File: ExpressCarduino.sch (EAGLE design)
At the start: 14 parts, among them IC1 MCP23017ML, U1 AP3012

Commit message: I keep tweaking the board...
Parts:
- renumbered U$2 to IC2
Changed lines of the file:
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@@
 <part name="GND5" library="supply1" deviceset="GND" device=""/>
 <part name="GPIO" library="SparkFun-Connectors" deviceset="M08" device=""/>
-<part name="U$2" library="HokieGeek" deviceset="SN74LV4051A" device=""/>
+<part name="IC2" library="HokieGeek" deviceset="SN74LV4051A" device=""/>
 <part name="ADC" library="SparkFun-Connectors" deviceset="M08" device=""/>
 <part name="IC1" library="adafruit" deviceset="MCP23017" device="ML"/>
@@
 <instance part="GND5" gate="1" x="127" y="76.2"/>
 <instance part="GPIO" gate="G$1" x="88.9" y="104.14" rot="R180"/>
-<instance part="U$2" gate="G$1" x="127" y="99.06"/>
+<instance part="IC2" gate="G$1" x="127" y="99.06"/>
 <instance part="ADC" gate="G$1" x="147.32" y="101.6" rot="R180"/>
 <instance part="IC1" gate="G$1" x="68.58" y="88.9"/>
@@
 </segment>
 <segment>
-<pinref part="U$2" gate="G$1" pin="VCC"/>
+<pinref part="IC2" gate="G$1" pin="VCC"/>
 <wire x1="127" y1="116.84" x2="127" y2="119.38" width="0.1524" layer="91"/>
 <label x="127" y="119.38" size="1.778" layer="95"/>
@@
 </segment>
 <segment>
-<pinref part="U$2" gate="G$1" pin="GND"/>
+<pinref part="IC2" gate="G$1" pin="GND"/>
 <pinref part="GND5" gate="1" pin="GND"/>
 <wire x1="127" y1="78.74" x2="127" y2="81.28" width="0.1524" layer="91"/>
@@
 </segment>
 <segment>
-<pinref part="U$2" gate="G$1" pin="!EN"/>
+<pinref part="IC2" gate="G$1" pin="!EN"/>
 <wire x1="111.76" y1="88.9" x2="106.68" y2="88.9" width="0.1524" layer="91"/>
 <label x="104.14" y="88.9" size="1.778" layer="95"/>
@@
 <net name="N$19" class="0">
 <segment>
-<pinref part="U$2" gate="G$1" pin="Y0"/>
+<pinref part="IC2" gate="G$1" pin="Y0"/>
 <pinref part="ADC" gate="G$1" pin="1"/>
 </segment>
@@
 <net name="N$20" class="0">
 <segment>
-<pinref part="U$2" gate="G$1" pin="Y1"/>
+<pinref part="IC2" gate="G$1" pin="Y1"/>
 <pinref part="ADC" gate="G$1" pin="2"/>
 </segment>
@@
 <net name="N$21" class="0">
 <segment>
-<pinref part="U$2" gate="G$1" pin="Y2"/>
+<pinref part="IC2" gate="G$1" pin="Y2"/>
 <pinref part="ADC" gate="G$1" pin="3"/>
 </segment>
@@
 <net name="N$22" class="0">
 <segment>
-<pinref part="U$2" gate="G$1" pin="Y3"/>
+<pinref part="IC2" gate="G$1" pin="Y3"/>
 <pinref part="ADC" gate="G$1" pin="4"/>
 </segment>
@@
 <net name="N$23" class="0">
 <segment>
-<pinref part="U$2" gate="G$1" pin="Y4"/>
+<pinref part="IC2" gate="G$1" pin="Y4"/>
 <pinref part="ADC" gate="G$1" pin="5"/>
 </segment>
@@
 <net name="N$24" class="0">
 <segment>
-<pinref part="U$2" gate="G$1" pin="Y5"/>
+<pinref part="IC2" gate="G$1" pin="Y5"/>
 <pinref part="ADC" gate="G$1" pin="6"/>
 </segment>
@@
 <net name="N$25" class="0">
 <segment>
-<pinref part="U$2" gate="G$1" pin="Y6"/>
+<pinref part="IC2" gate="G$1" pin="Y6"/>
 <pinref part="ADC" gate="G$1" pin="7"/>
 </segment>
@@
 <net name="N$26" class="0">
 <segment>
-<pinref part="U$2" gate="G$1" pin="Y7"/>
+<pinref part="IC2" gate="G$1" pin="Y7"/>
 <pinref part="ADC" gate="G$1" pin="8"/>
 </segment>
@@
 </segment>
 <segment>
-<pinref part="U$2" gate="G$1" pin="COM"/>
+<pinref part="IC2" gate="G$1" pin="COM"/>
 <wire x1="109.22" y1="96.52" x2="111.76" y2="96.52" width="0.1524" layer="91"/>
 <label x="99.06" y="96.52" size="1.778" layer="95"/>
@@
 <net name="MUX_A" class="0">
 <segment>
-<pinref part="U$2" gate="G$1" pin="A"/>
+<pinref part="IC2" gate="G$1" pin="A"/>
 <wire x1="111.76" y1="109.22" x2="109.22" y2="109.22" width="0.1524" layer="91"/>
 <label x="104.14" y="109.22" size="1.778" layer="95"/>
@@
 <net name="MUX_B" class="0">
 <segment>
-<pinref part="U$2" gate="G$1" pin="B"/>
+<pinref part="IC2" gate="G$1" pin="B"/>
 <wire x1="111.76" y1="106.68" x2="109.22" y2="106.68" width="0.1524" layer="91"/>
 <label x="104.14" y="106.68" size="1.778" layer="95"/>
@@
 <net name="MUX_C" class="0">
 <segment>
-<pinref part="U$2" gate="G$1" pin="C"/>
+<pinref part="IC2" gate="G$1" pin="C"/>
 <wire x1="111.76" y1="104.14" x2="109.22" y2="104.14" width="0.1524" layer="91"/>
 <label x="104.14" y="104.14" size="1.778" layer="95"/>

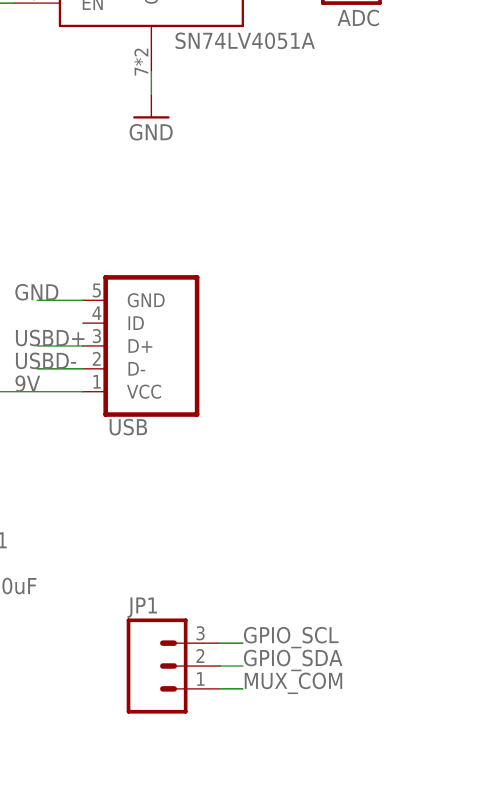
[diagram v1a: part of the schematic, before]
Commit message: Added power supply pins based on #10
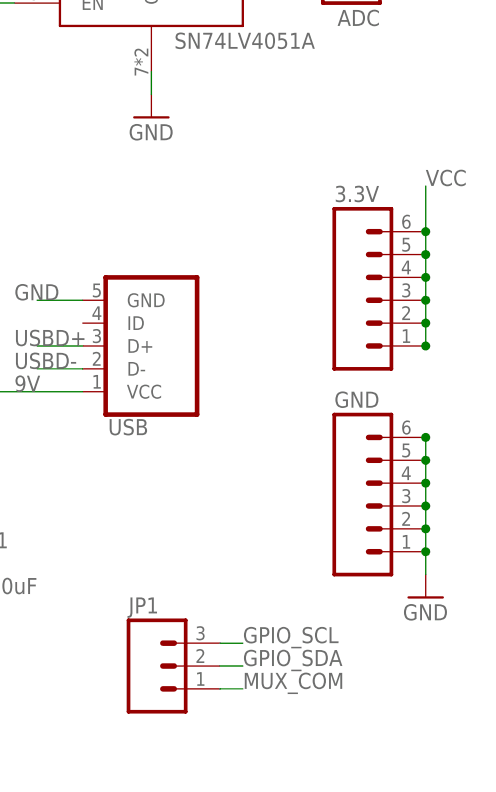
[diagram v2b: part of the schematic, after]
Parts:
- added 3.3V, GND: (no value), SparkFun-Connectors:M06SILK_FEMALE_PTH
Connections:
- net GND: now also GND.1, GND.2, GND.3, GND.4, GND.5, GND.6
- net VCC: now also 3.3V.1, 3.3V.2, 3.3V.3, 3.3V.4, 3.3V.5, 3.3V.6
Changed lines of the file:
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@@
 <part name="IC1" library="adafruit" deviceset="MCP23017" device="ML"/>
 <part name="JP1" library="SparkFun-Connectors" deviceset="M03" device="PTH"/>
+<part name="3.3V" library="SparkFun-Connectors" deviceset="M06" device="SILK_FEMALE_PTH"/>
+<part name="GND" library="SparkFun-Connectors" deviceset="M06" device="SILK_FEMALE_PTH"/>
+<part name="GND2" library="supply1" deviceset="GND" device=""/>
 </parts>
 <sheets>
@@
 <instance part="IC1" gate="G$1" x="68.58" y="88.9"/>
 <instance part="JP1" gate="G$1" x="127" y="15.24"/>
+<instance part="3.3V" gate="G$1" x="152.4" y="55.88"/>
+<instance part="GND" gate="G$1" x="152.4" y="33.02"/>
+<instance part="GND2" gate="1" x="157.48" y="22.86"/>
 </instances>
 <busses>
@@
 <wire x1="53.34" y1="104.14" x2="53.34" y2="109.22" width="0.1524" layer="91"/>
 <junction x="53.34" y="109.22"/>
+</segment>
+<segment>
+<pinref part="3.3V" gate="G$1" pin="1"/>
+<pinref part="3.3V" gate="G$1" pin="2"/>
+<wire x1="157.48" y1="50.8" x2="157.48" y2="53.34" width="0.1524" layer="91"/>
+<pinref part="3.3V" gate="G$1" pin="3"/>
+<wire x1="157.48" y1="53.34" x2="157.48" y2="55.88" width="0.1524" layer="91"/>
+<pinref part="3.3V" gate="G$1" pin="4"/>
+<wire x1="157.48" y1="55.88" x2="157.48" y2="58.42" width="0.1524" layer="91"/>
+<pinref part="3.3V" gate="G$1" pin="5"/>
+<wire x1="157.48" y1="58.42" x2="157.48" y2="60.96" width="0.1524" layer="91"/>
+<pinref part="3.3V" gate="G$1" pin="6"/>
+<wire x1="157.48" y1="60.96" x2="157.48" y2="63.5" width="0.1524" layer="91"/>
+<wire x1="157.48" y1="63.5" x2="157.48" y2="68.58" width="0.1524" layer="91"/>
+<label x="157.48" y="68.58" size="1.778" layer="95"/>
+<junction x="157.48" y="50.8"/>
+<junction x="157.48" y="53.34"/>
+<junction x="157.48" y="55.88"/>
+<junction x="157.48" y="58.42"/>
+<junction x="157.48" y="60.96"/>
+<junction x="157.48" y="63.5"/>
 </segment>
 </net>
@@
 <junction x="53.34" y="76.2"/>
 </segment>
+<segment>
+<pinref part="GND2" gate="1" pin="GND"/>
+<pinref part="GND" gate="G$1" pin="1"/>
+<wire x1="157.48" y1="25.4" x2="157.48" y2="27.94" width="0.1524" layer="91"/>
+<pinref part="GND" gate="G$1" pin="2"/>
+<wire x1="157.48" y1="27.94" x2="157.48" y2="30.48" width="0.1524" layer="91"/>
+<pinref part="GND" gate="G$1" pin="3"/>
+<wire x1="157.48" y1="30.48" x2="157.48" y2="33.02" width="0.1524" layer="91"/>
+<pinref part="GND" gate="G$1" pin="4"/>
+<wire x1="157.48" y1="33.02" x2="157.48" y2="35.56" width="0.1524" layer="91"/>
+<pinref part="GND" gate="G$1" pin="5"/>
+<wire x1="157.48" y1="35.56" x2="157.48" y2="38.1" width="0.1524" layer="91"/>
+<pinref part="GND" gate="G$1" pin="6"/>
+<wire x1="157.48" y1="38.1" x2="157.48" y2="40.64" width="0.1524" layer="91"/>
+<junction x="157.48" y="27.94"/>
+<junction x="157.48" y="30.48"/>
+<junction x="157.48" y="33.02"/>
+<junction x="157.48" y="35.56"/>
+<junction x="157.48" y="38.1"/>
+<junction x="157.48" y="40.64"/>
+</segment>
 </net>

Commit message: Trying things out
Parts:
- added IC3: MCP23008, HokieGeek:MCP23008
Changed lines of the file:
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@@
 <layer number="255" name="routoute" color="7" fill="1" visible="yes" active="yes"/>
 </layers>
-<schematic xreflabel="%F%N/%S.%C%R" xrefpart="/%S.%C%R">
+<schematic xreflabel="%F%N/%S" xrefpart="/%S">
 <attributes>
 </attributes>
@@
 <part name="GND" library="SparkFun-Connectors" deviceset="M06" device="SILK_FEMALE_PTH"/>
 <part name="GND2" library="supply1" deviceset="GND" device=""/>
+<part name="IC3" library="HokieGeek" deviceset="MCP23008" device=""/>
 </parts>
 <sheets>
@@
 <instance part="GND" gate="G$1" x="152.4" y="33.02"/>
 <instance part="GND2" gate="1" x="157.48" y="22.86"/>
+<instance part="IC3" gate="G$1" x="68.58" y="139.7"/>
 </instances>
 <busses>

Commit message: Modified current schematic to remove potential nogo and added "basic" board
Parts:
- removed IC3: MCP23008, HokieGeek:MCP23008
- IC2: value SN74LV4051A -> SN74LV4051APWR; device HokieGeek:SN74LV4051A -> HokieGeek:SN74LV4051APWR
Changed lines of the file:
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@@
 <?xml version="1.0" encoding="utf-8"?>
 <!DOCTYPE eagle SYSTEM "eagle.dtd">
-<eagle version="7.4.0">
+<eagle version="9.1.2">
 <drawing>
 <settings>
 <setting alwaysvectorfont="no"/>
+<setting keepoldvectorfont="yes"/>
 <setting verticaltext="up"/>
 </settings>
@@
 <part name="R1" library="SparkFun-Resistors" deviceset="0.22OHM-1/4W-1%(0805)" device="" value="41.2K"/>
 <part name="R2" library="SparkFun-Resistors" deviceset="0.22OHM-1/4W-1%(0805)" device="" value="6.5K"/>
-<part name="GND1" library="supply1" deviceset="GND" device=""/>
+<part name="GND1" library="supply1" library_urn="urn:adsk.eagle:library:371" deviceset="GND" device=""/>
 <part name="U1" library="HokieGeek" deviceset="AP3012" device="" value="AP3012"/>
-<part name="C1" library="SparkFun-Capacitors" deviceset="1.0UF-16V-10%(0603)" device="" value="1.0uF"/>
-<part name="C2" library="SparkFun-Capacitors" deviceset="1.0UF-16V-10%(0603)" device="" value="1.0uF"/>
+<part name="C1" library="SparkFun-Capacitors" library_urn="urn:adsk.eagle:library:510" deviceset="1.0UF-16V-10%(0603)" device="" value="1.0uF"/>
+<part name="C2" library="SparkFun-Capacitors" library_urn="urn:adsk.eagle:library:510" deviceset="1.0UF-16V-10%(0603)" device="" value="1.0uF"/>
 <part name="L1" library="SparkFun-Passives" deviceset="INDUCTOR" device="SDR0403-560KL" value="56uH"/>
 <part name="D1" library="HokieGeek" deviceset="DIODE-SCHOTTKY" device="" value="1N5819"/>
 <part name="USB" library="HokieGeek" deviceset="USB_MICROB_PLUG" device="&quot;"/>
-<part name="GND4" library="supply1" deviceset="GND" device=""/>
-<part name="GND5" library="supply1" deviceset="GND" device=""/>
+<part name="GND4" library="supply1" library_urn="urn:adsk.eagle:library:371" deviceset="GND" device=""/>
+<part name="GND5" library="supply1" library_urn="urn:adsk.eagle:library:371" deviceset="GND" device=""/>
 <part name="GPIO" library="SparkFun-Connectors" deviceset="M08" device=""/>
-<part name="IC2" library="HokieGeek" deviceset="SN74LV4051A" device=""/>
+<part name="IC2" library="HokieGeek" deviceset="SN74LV4051A" device="PWR"/>
 <part name="ADC" library="SparkFun-Connectors" deviceset="M08" device=""/>
-<part name="IC1" library="adafruit" deviceset="MCP23017" device="ML"/>
+<part name="IC1" library="adafruit" library_urn="urn:adsk.eagle:library:420" deviceset="MCP23017" device="ML"/>
 <part name="JP1" library="SparkFun-Connectors" deviceset="M03" device="PTH"/>
 <part name="3.3V" library="SparkFun-Connectors" deviceset="M06" device="SILK_FEMALE_PTH"/>
 <part name="GND" library="SparkFun-Connectors" deviceset="M06" device="SILK_FEMALE_PTH"/>
-<part name="GND2" library="supply1" deviceset="GND" device=""/>
-<part name="IC3" library="HokieGeek" deviceset="MCP23008" device=""/>
+<part name="GND2" library="supply1" library_urn="urn:adsk.eagle:library:371" deviceset="GND" device=""/>
 </parts>
 <sheets>
@@
 <instance part="GND" gate="G$1" x="152.4" y="33.02"/>
 <instance part="GND2" gate="1" x="157.48" y="22.86"/>
-<instance part="IC3" gate="G$1" x="68.58" y="139.7"/>
 </instances>
 <busses>
@@
 </schematic>
 </drawing>
+<compatibility>
+<note version="8.2" severity="warning">
+Since Version 8.2, EAGLE supports online libraries. The ids
+of those online libraries will not be understood (or retained)
+with this version.
+</note>
+<note version="8.3" severity="warning">
+Since Version 8.3, EAGLE supports URNs for individual library
+assets (packages, symbols, and devices). The URNs of those assets
+will not be understood (or retained) with this version.
+</note>
+</compatibility>
 </eagle>
